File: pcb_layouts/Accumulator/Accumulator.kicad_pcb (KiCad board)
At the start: 2 copper layers, 135 x 120 mm, 32 parts, among them J1 Conn_02x20_Odd_Even, J2 Conn_02x20_Odd_Even, U1 74LS173, U10 74LS245, U11 74LS245, U12 74LS245, U2 74LS173, U3 74LS173, U4 74LS173, U5 74LS173, U6 74LS173, U7 74LS173, U8 74LS173, U9 74LS245

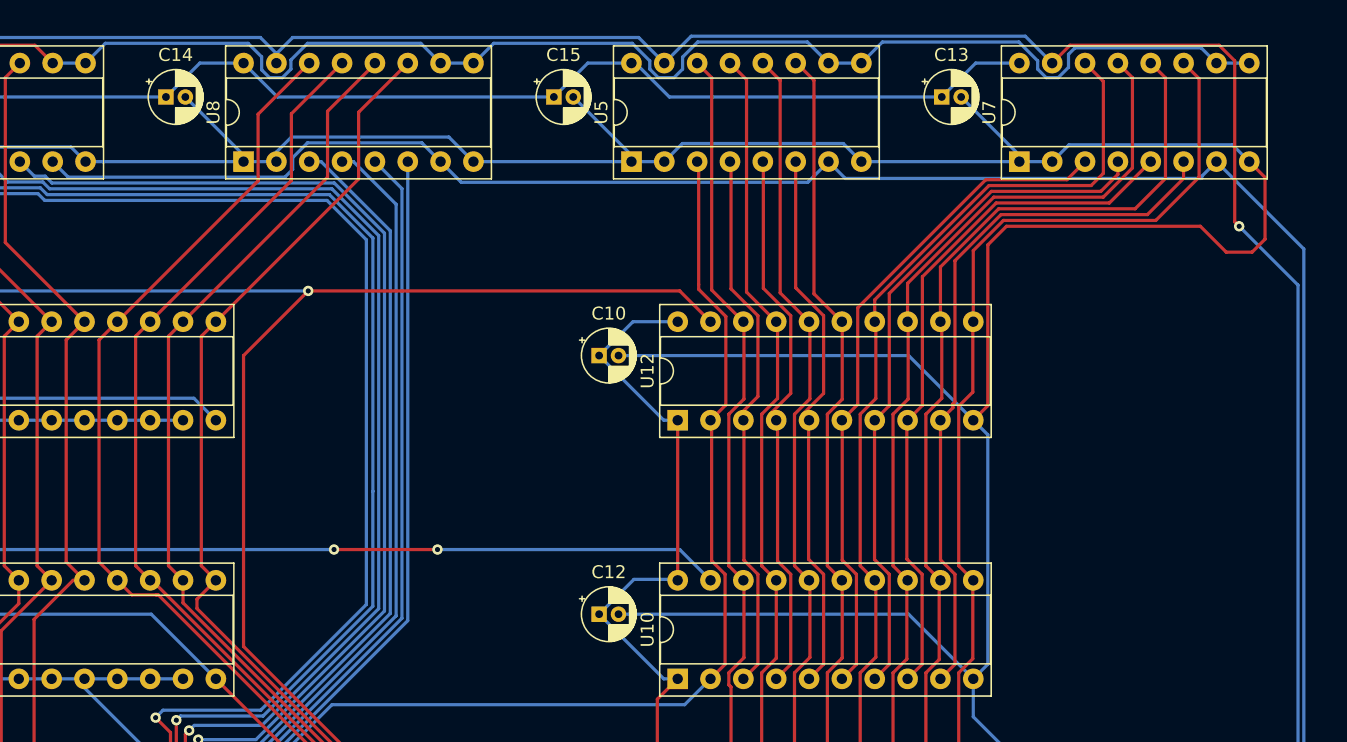
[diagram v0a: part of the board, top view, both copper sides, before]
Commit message: Figuring out variables, added pcb layout for PC
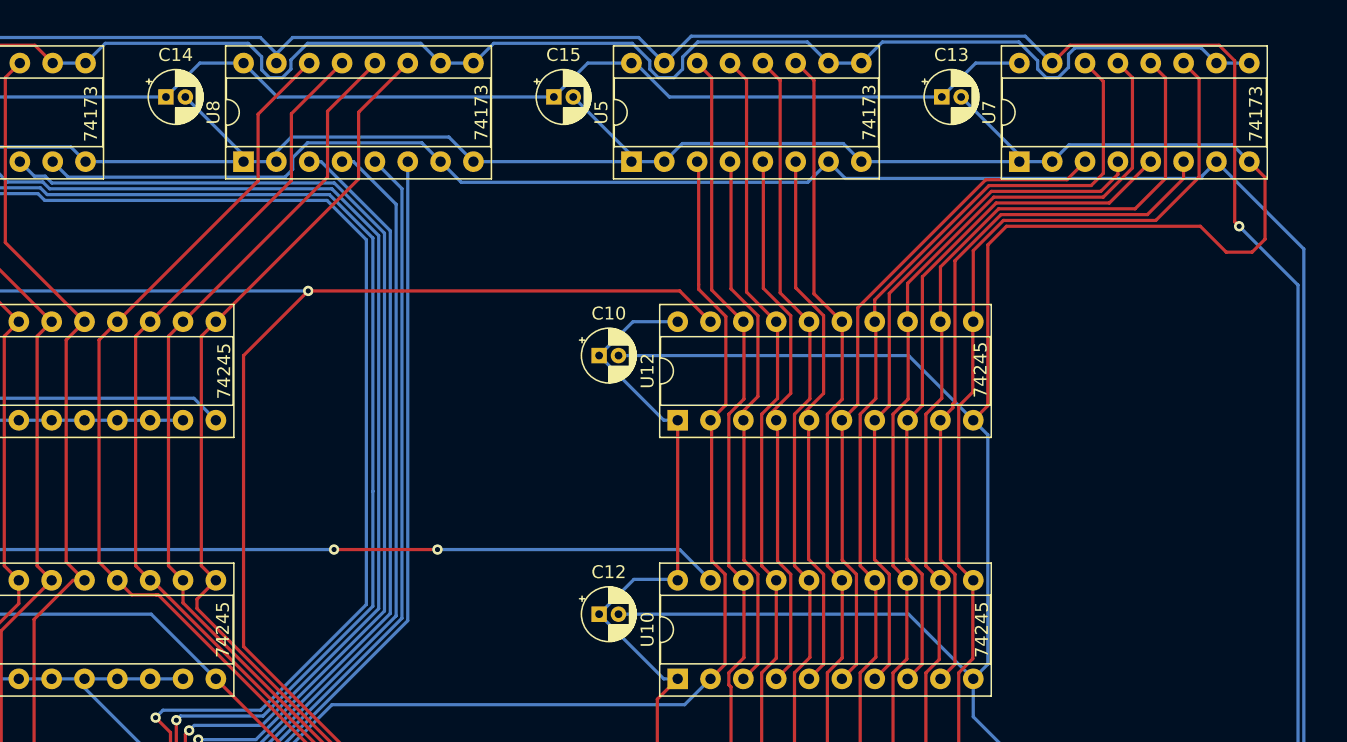
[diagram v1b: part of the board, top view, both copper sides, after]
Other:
- board text added: "74245"
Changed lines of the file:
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@@
   (gr_arc (start 190 154) (mid 189.707107 154.707107) (end 189 155) (layer "Edge.Cuts") (width 0.1))
   (gr_arc (start 57 155) (mid 55.585786 154.414214) (end 55 153) (layer "Edge.Cuts") (width 0.1))
+  (gr_text "74245" (at 98.4 101.2 90) (layer "F.SilkS")
+    (effects (font (size 1 1) (thickness 0.15)))
+  )
+  (gr_text "74245" (at 157 81.1 90) (layer "F.SilkS")
+    (effects (font (size 1 1) (thickness 0.15)))
+  )
   (gr_text "74173" (at 89.3 124.9 90) (layer "F.SilkS")
+    (effects (font (size 1 1) (thickness 0.15)))
+  )
+  (gr_text "74245" (at 157.1 101.2 90) (layer "F.SilkS")
     (effects (font (size 1 1) (thickness 0.15)))
   )
@@
     (effects (font (size 1 1) (thickness 0.15)))
   )
+  (gr_text "74173" (at 148.4 61.2 90) (layer "F.SilkS")
+    (effects (font (size 1 1) (thickness 0.15)))
+  )
+  (gr_text "74173" (at 88.2 61.3 90) (layer "F.SilkS")
+    (effects (font (size 1 1) (thickness 0.15)))
+  )
+  (gr_text "74245" (at 98.5 81.2 90) (layer "F.SilkS")
+    (effects (font (size 1 1) (thickness 0.15)))
+  )
   (gr_text "0.1uf" (at 73.2 118.3) (layer "F.SilkS")
+    (effects (font (size 1 1) (thickness 0.15)))
+  )
+  (gr_text "74173" (at 178.3 61.3 90) (layer "F.SilkS")
     (effects (font (size 1 1) (thickness 0.15)))
   )
@@
     (effects (font (size 1 1) (thickness 0.15)))
   )
+  (gr_text "74173" (at 118.4 61.2 90) (layer "F.SilkS")
+    (effects (font (size 1 1) (thickness 0.15)))
+  )
